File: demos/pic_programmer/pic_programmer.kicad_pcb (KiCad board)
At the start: 2 copper layers, 160 x 99.1 mm, 63 parts, among them J1 DB9-FEMAL, P1 CONN_2, P101 CONN_1, P102 CONN_1, P103 CONN_1, P104 CONN_1, P105 CONN_1, P106 CONN_1, P2 SUPP28, P3 SUPP40, Q1 BC237, Q2 BC307, Q3 BC307, U1 24Cxx, U2 74HC125, U3 7805, U4 LT1373, U5 PIC_18_PINS, U6 PIC_8_PINS

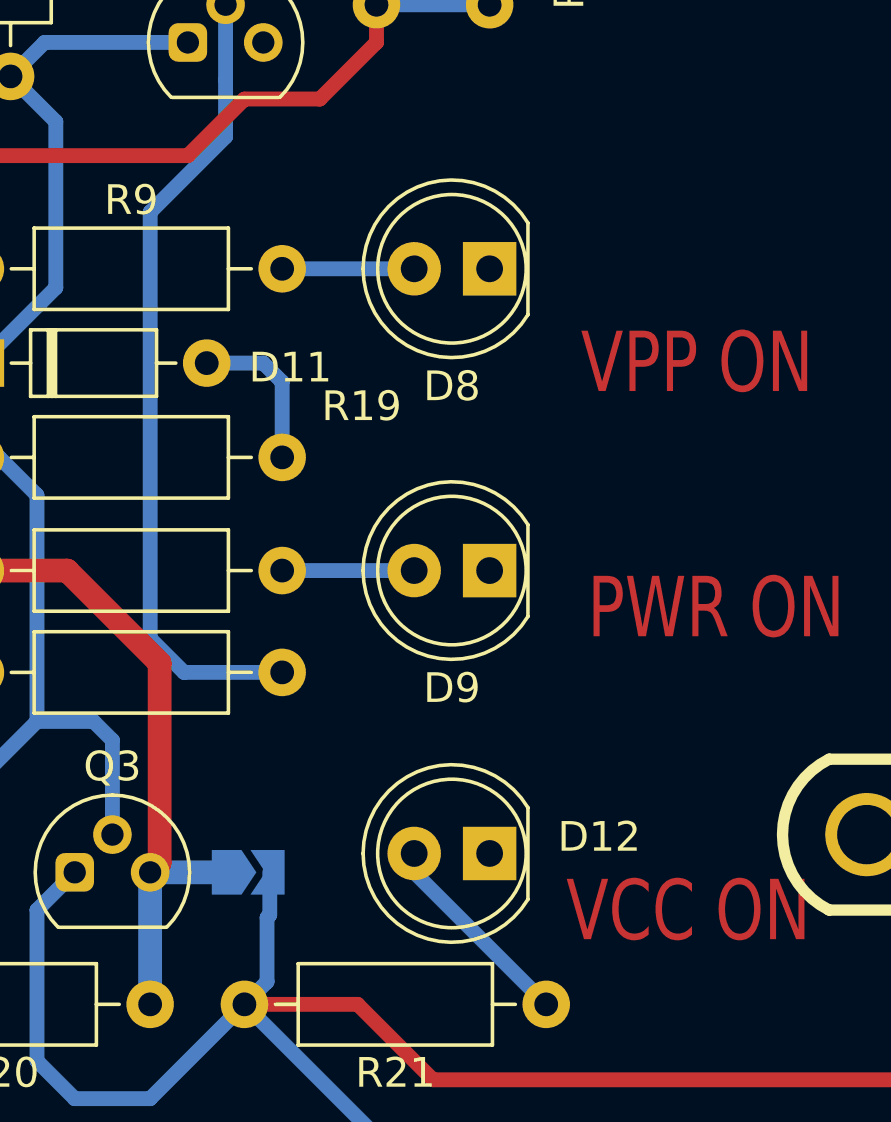
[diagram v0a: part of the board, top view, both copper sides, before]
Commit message: feat: update kicad to 9.0.0+dfsg-1
Signed-off-by: lhdjply <lhdjply@126.com>
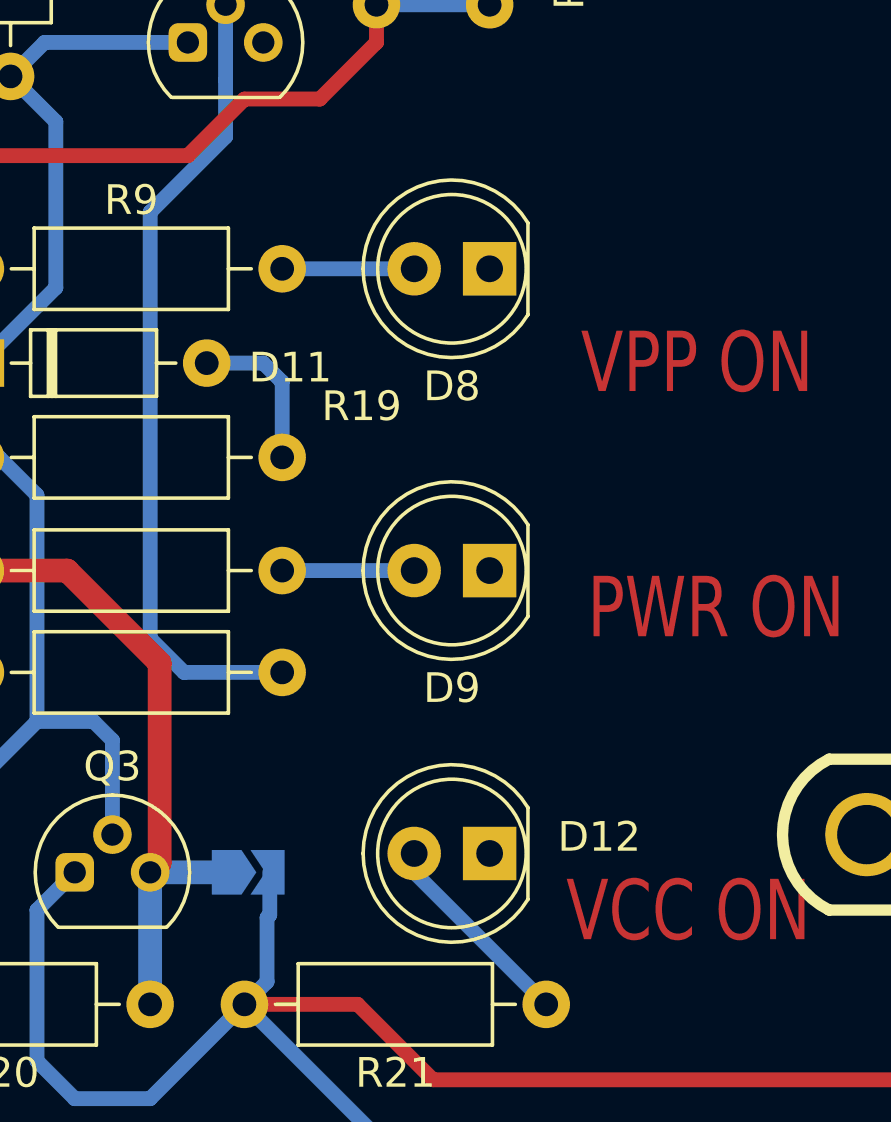
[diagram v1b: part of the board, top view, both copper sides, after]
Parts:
- C1, C2: footprint Capacitor_THT:CP_Axial_L18.0mm_D6.5mm_P25.00mm_Horizontal -> footprints:CP_Axial_L18.0mm_D6.5mm_P25.00mm_Horizontal
- C3: footprint Capacitor_THT:C_Axial_L12.0mm_D6.5mm_P20.00mm_Horizontal -> footprints:C_Axial_L12.0mm_D6.5mm_P20.00mm_Horizontal
- C4, C5, C6, C7, C9: footprint Capacitor_THT:C_Disc_D5.1mm_W3.2mm_P5.00mm -> footprints:C_Disc_D5.1mm_W3.2mm_P5.00mm
- D1, D10: footprint Diode_THT:D_DO-35_SOD27_P12.70mm_Horizontal -> footprints:D_DO-35_SOD27_P12.70mm_Horizontal
- D11, D2, D3, D4, D5, D6, D7: footprint Diode_THT:D_DO-35_SOD27_P7.62mm_Horizontal -> footprints:D_DO-35_SOD27_P7.62mm_Horizontal
- D12, D8, D9: footprint LED_THT:LED_D5.0mm -> footprints:LED_D5.0mm
- J1: footprint Connector_Dsub:DSUB-9_Female_Horizontal_P2.77x2.84mm_EdgePinOffset7.70mm_Housed_MountingHolesOffset9.12mm -> footprints:DSUB-9_Female_Horizontal_P2.77x2.84mm_EdgePinOffset7.70mm_Housed_MountingHolesOffset9.12mm
- JP1: footprint Jumper:SolderJumper-2_P1.3mm_Open_TrianglePad1.0x1.5mm -> footprints:SolderJumper-2_P1.3mm_Open_TrianglePad1.0x1.5mm
- L1: footprint Inductor_THT:L_Radial_D7.8mm_P5.00mm_Fastron_07HCP -> footprints:L_Radial_D7.8mm_P5.00mm_Fastron_07HCP
- P1: footprint TerminalBlock_Altech:Altech_AK300_1x02_P5.00mm_45-Degree -> footprints:Altech_AK300_1x02_P5.00mm_45-Degree
- P101, P102, P103, P104, P105, P106: footprint MountingHole:MountingHole_4.3mm_M4 -> footprints:MountingHole_4.3mm_M4
- P2: footprint Package_DIP:DIP-28_W7.62mm_Socket_LongPads -> footprints:DIP-28_W7.62mm_Socket_LongPads
- Q1, Q2, Q3: footprint Package_TO_SOT_THT:TO-92 -> footprints:TO-92
- R1, R10, R11, R12, R13, R14, R15, R16, R17, R18, R19, R2, R20, R21, R3, R4, R5, R6, R7, R8, R9: footprint Resistor_THT:R_Axial_DIN0207_L6.3mm_D2.5mm_P10.16mm_Horizontal -> footprints:R_Axial_DIN0207_L6.3mm_D2.5mm_P10.16mm_Horizontal
- U1, U6: footprint Package_DIP:DIP-8_W7.62mm_Socket_LongPads -> footprints:DIP-8_W7.62mm_Socket_LongPads
- U2: footprint Package_DIP:DIP-14_W7.62mm_LongPads -> footprints:DIP-14_W7.62mm_LongPads
- U3: footprint Package_TO_SOT_THT:TO-220-3_Horizontal_TabDown -> footprints:TO-220-3_Horizontal_TabDown
- U4: footprint Package_DIP:DIP-8_W7.62mm_LongPads -> footprints:DIP-8_W7.62mm_LongPads
- U5: footprint Package_DIP:DIP-18_W7.62mm_Socket_LongPads -> footprints:DIP-18_W7.62mm_Socket_LongPads
